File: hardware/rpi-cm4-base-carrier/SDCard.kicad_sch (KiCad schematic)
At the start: 4 parts, among them J14 DM3CS-SF, U4 RT9742GGJ5

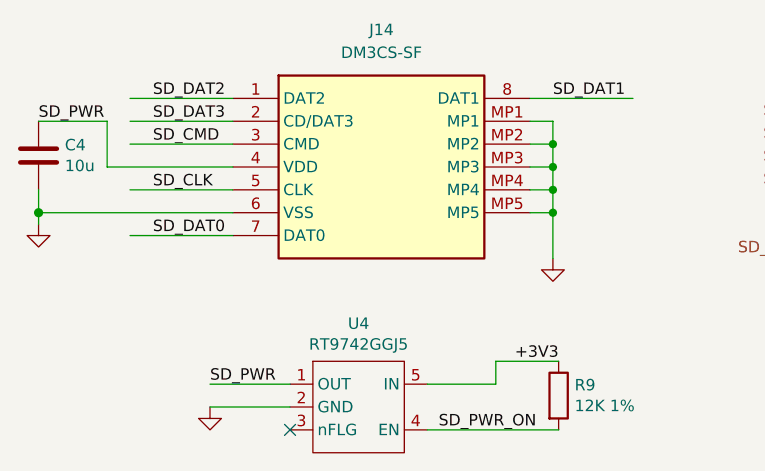
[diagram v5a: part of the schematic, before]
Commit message: convert IC refs to U refs and re-annotate, add fiducials and extra via stitching to layout
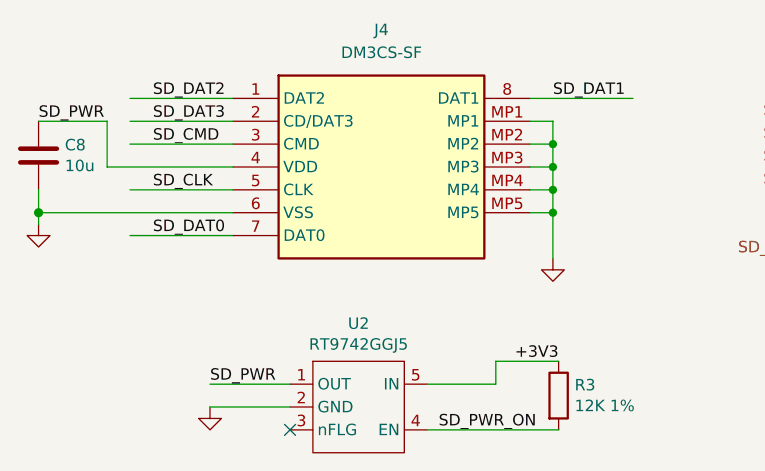
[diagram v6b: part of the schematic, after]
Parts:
- renumbered C4 to C8, J14 to J4, R9 to R3, U4 to U2
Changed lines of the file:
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@@
   (symbol (lib_id "SamacSys_Parts:DM3CS-SF") (at 92.71 31.75 0) (unit 1)
     (in_bom yes) (on_board yes) (dnp no) (fields_autoplaced)
-    (property "Reference" "J14" (at 109.22 24.13 0)
+    (property "Reference" "J4" (at 109.22 24.13 0)
       (effects (font (size 1.27 1.27)))
     )
@@
       (project "rpi-cm4-base-carrier"
         (path "/92c58705-ecb0-498b-b561-44a3f0daad57/26b25ff9-f711-41bc-bcf8-c3ce0c6a0e37"
-          (reference "J14") (unit 1)
+          (reference "J4") (unit 1)
         )
       )
@@
   (symbol (lib_id "CM4IO:RT9742GGJ5") (at 107.95 73.66 0) (unit 1)
     (in_bom yes) (on_board yes) (dnp no)
-    (property "Reference" "U4" (at 106.68 56.769 0)
+    (property "Reference" "U2" (at 106.68 56.769 0)
       (effects (font (size 1.27 1.27)))
     )
@@
       (project "rpi-cm4-base-carrier"
         (path "/92c58705-ecb0-498b-b561-44a3f0daad57/26b25ff9-f711-41bc-bcf8-c3ce0c6a0e37"
-          (reference "U4") (unit 1)
+          (reference "U2") (unit 1)
         )
       )
@@
   (symbol (lib_id "Device:R") (at 128.905 64.77 0) (unit 1)
     (in_bom yes) (on_board yes) (dnp no)
-    (property "Reference" "R9" (at 130.683 63.6016 0)
+    (property "Reference" "R3" (at 130.683 63.6016 0)
       (effects (font (size 1.27 1.27)) (justify left))
     )
@@
       (project "rpi-cm4-base-carrier"
         (path "/92c58705-ecb0-498b-b561-44a3f0daad57/26b25ff9-f711-41bc-bcf8-c3ce0c6a0e37"
-          (reference "R9") (unit 1)
+          (reference "R3") (unit 1)
         )
       )
@@
   (symbol (lib_id "Device:C") (at 71.12 38.1 0) (unit 1)
     (in_bom yes) (on_board yes) (dnp no)
-    (property "Reference" "C4" (at 74.041 36.9316 0)
+    (property "Reference" "C8" (at 74.041 36.9316 0)
       (effects (font (size 1.27 1.27)) (justify left))
     )
@@
       (project "rpi-cm4-base-carrier"
         (path "/92c58705-ecb0-498b-b561-44a3f0daad57/26b25ff9-f711-41bc-bcf8-c3ce0c6a0e37"
-          (reference "C4") (unit 1)
-        )
-      )
+          (reference "C8") (unit 1)
+        )
+      )

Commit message: design files exported ready for manufacture, LCSC part numbers added throughout the library
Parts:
- C8: LCSC Part # (none) -> C326595; LCSC Part Number (none) -> C326595
- J4: LCSC Part # (none) -> C202111; LCSC Part Number (none) -> C202111
- R3: LCSC Part # (none) -> C186350; LCSC Part Number (none) -> C186350
- U2: LCSC Part # (none) -> C250547; LCSC Part Number (none) -> C250547
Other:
- title: (none) -> Raspberry Pi Compute Module 4 Control Node
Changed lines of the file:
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@@
 (kicad_sch (version 20230121) (generator eeschema)
   (paper "A4")
+  (title_block
+    (title "Raspberry Pi Compute Module 4 Control Node")
+    (date "2024-02-04")
+    (comment 2 "creativecommons.org/licenses/by-sa/4.0/")
+    (comment 3 "License: CC BY-SA 4.0")
+    (comment 4 "Author: Sam Earnshaw")
+  )
   (junction (at 128.27 36.83) (diameter 0) (color 0 0 0 0)
   )
@@
     (property "Manufacturer_Part_Number" "DM3CS-SF" (at 121.92 826.67 0)
       (effects (font (size 1.27 1.27)) (justify left top) hide)
+    )
+    (property "LCSC Part Number" "C202111" (at 92.71 31.75 0)
+      (effects (font (size 1.27 1.27)) hide)
+    )
+    (property "LCSC Part #" "C202111" (at 92.71 31.75 0)
+      (effects (font (size 1.27 1.27)) hide)
     )
     (pin "MP5")
@@
       (effects (font (size 1.27 1.27)) hide)
     )
+    (property "LCSC Part Number" "C250547" (at 107.95 73.66 0)
+      (effects (font (size 1.27 1.27)) hide)
+    )
+    (property "LCSC Part #" "C250547" (at 107.95 73.66 0)
+      (effects (font (size 1.27 1.27)) hide)
+    )
     (pin "1")
     (pin "2")
@@
       (effects (font (size 1.27 1.27)) hide)
     )
+    (property "LCSC Part Number" "C186350" (at 128.905 64.77 0)
+      (effects (font (size 1.27 1.27)) hide)
+    )
+    (property "LCSC Part #" "C186350" (at 128.905 64.77 0)
+      (effects (font (size 1.27 1.27)) hide)
+    )
     (pin "1")
     (pin "2")
@@
       (effects (font (size 1.27 1.27)) hide)
     )
+    (property "LCSC Part Number" "C326595" (at 71.12 38.1 0)
+      (effects (font (size 1.27 1.27)) hide)
+    )
+    (property "LCSC Part #" "C326595" (at 71.12 38.1 0)
+      (effects (font (size 1.27 1.27)) hide)
+    )
